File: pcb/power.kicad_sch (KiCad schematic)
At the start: 29 parts, among them J2 USB_C_Top, J3 USB_C_Bottom, Q2 AO3401A, U2 TPS63000, U3 TPS63000, U4 TP4056

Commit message: style: schematics cleanup
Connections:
- net VBUS renamed V_{BUS}
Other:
- note added: "3.3V"
- note added: "5.0V"
- note added: "Battery Charger"
- note added: "Power Input"
- note added: "Power Sharing"
- moved on the sheet: BT1, C10, C11, C12, C8, C9, J2, J3, L1, L2, R12, R13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

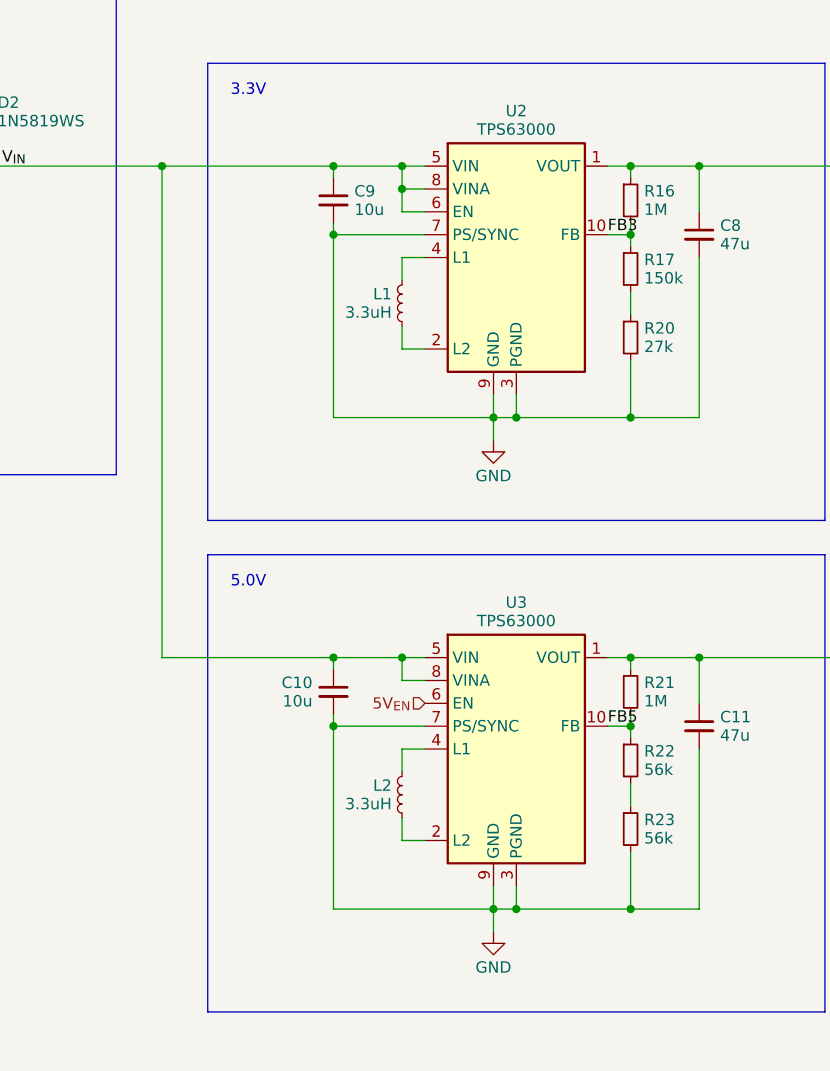
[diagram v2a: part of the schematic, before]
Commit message: style: add 3d models for pcb render
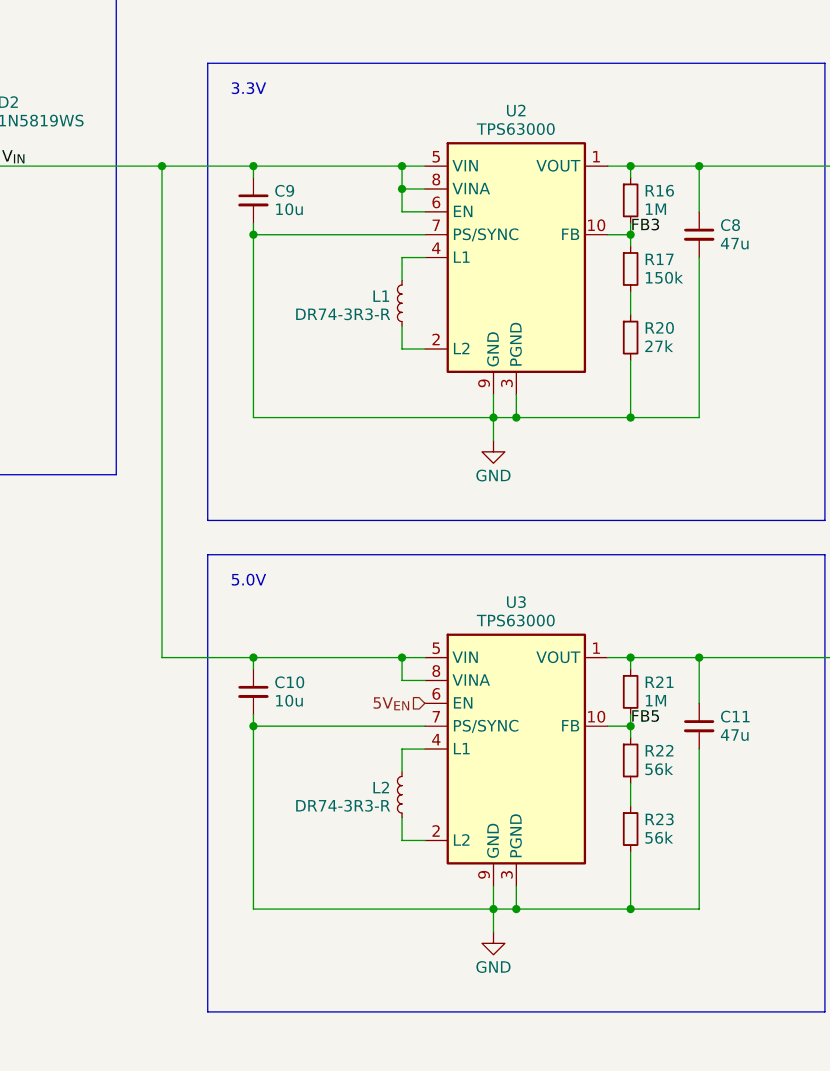
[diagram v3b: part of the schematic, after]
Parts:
- L1, L2: value 3.3uH -> DR74-3R3-R
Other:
- moved on the sheet: C10, C9
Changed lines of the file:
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@@
     (rev "${VERSION}")
   )
-  (junction (at 217.17 49.53) (diameter 0) (color 0 0 0 0)
-  )
   (junction (at 224.79 52.07) (diameter 0) (color 0 0 0 0)
   )
   (junction (at 257.81 104.14) (diameter 0) (color 0 0 0 0)
   )
-  (junction (at 217.17 104.14) (diameter 0) (color 0 0 0 0)
+  (junction (at 208.28 104.14) (diameter 0) (color 0 0 0 0)
+  )
+  (junction (at 208.28 49.53) (diameter 0) (color 0 0 0 0)
   )
   (junction (at 99.06 62.23) (diameter 0) (color 0 0 0 0)
@@
   (junction (at 250.19 57.15) (diameter 0) (color 0 0 0 0)
   )
-  (junction (at 217.17 57.15) (diameter 0) (color 0 0 0 0)
+  (junction (at 208.28 57.15) (diameter 0) (color 0 0 0 0)
   )
   (junction (at 224.79 104.14) (diameter 0) (color 0 0 0 0)
   )
-  (junction (at 217.17 111.76) (diameter 0) (color 0 0 0 0)
+  (junction (at 208.28 111.76) (diameter 0) (color 0 0 0 0)
   )
   (junction (at 234.95 132.08) (diameter 0) (color 0 0 0 0)
@@
     (stroke (width 0) (type default))
   )
-  (wire (pts (xy 217.17 104.14) (xy 198.12 104.14))
+  (wire (pts (xy 208.28 104.14) (xy 198.12 104.14))
     (stroke (width 0) (type default))
   )
@@
     (stroke (width 0) (type default))
   )
-  (wire (pts (xy 247.65 57.15) (xy 250.19 57.15))
-    (stroke (width 0) (type default))
-  )
   (wire (pts (xy 60.96 101.6) (xy 55.88 101.6))
     (stroke (width 0) (type default))
@@
     (stroke (width 0) (type default))
   )
-  (wire (pts (xy 247.65 111.76) (xy 250.19 111.76))
-    (stroke (width 0) (type default))
-  )
   (wire (pts (xy 95.25 46.99) (xy 95.25 49.53))
     (stroke (width 0) (type default))
@@
     (stroke (width 0) (type default))
   )
-  (wire (pts (xy 217.17 57.15) (xy 217.17 77.47))
+  (wire (pts (xy 208.28 57.15) (xy 208.28 77.47))
     (stroke (width 0) (type default))
   )
@@
     (stroke (width 0) (type default))
   )
-  (wire (pts (xy 217.17 49.53) (xy 224.79 49.53))
-    (stroke (width 0) (type default))
-  )
   (wire (pts (xy 177.8 46.99) (xy 177.8 49.53))
     (stroke (width 0) (type default))
@@
     (stroke (width 0) (type default))
   )
-  (wire (pts (xy 217.17 55.88) (xy 217.17 57.15))
+  (wire (pts (xy 208.28 55.88) (xy 208.28 57.15))
     (stroke (width 0) (type default))
   )
@@
     (stroke (width 0) (type default))
   )
-  (wire (pts (xy 217.17 132.08) (xy 234.95 132.08))
+  (wire (pts (xy 208.28 132.08) (xy 234.95 132.08))
     (stroke (width 0) (type default))
   )
@@
     (stroke (width 0) (type default))
   )
-  (wire (pts (xy 217.17 49.53) (xy 217.17 50.8))
+  (wire (pts (xy 208.28 49.53) (xy 208.28 50.8))
     (stroke (width 0) (type default))
   )
@@
     (stroke (width 0) (type default))
   )
-  (wire (pts (xy 217.17 111.76) (xy 217.17 132.08))
+  (wire (pts (xy 250.19 111.76) (xy 247.65 111.76))
+    (stroke (width 0) (type default))
+  )
+  (wire (pts (xy 208.28 111.76) (xy 208.28 132.08))
     (stroke (width 0) (type default))
   )
@@
     (stroke (width 0) (type default))
   )
-  (wire (pts (xy 217.17 104.14) (xy 217.17 105.41))
+  (wire (pts (xy 208.28 104.14) (xy 208.28 105.41))
     (stroke (width 0) (type default))
   )
@@
     (stroke (width 0) (type default))
   )
-  (wire (pts (xy 217.17 111.76) (xy 227.33 111.76))
+  (wire (pts (xy 208.28 111.76) (xy 227.33 111.76))
     (stroke (width 0) (type default))
   )
@@
     (stroke (width 0) (type default))
   )
-  (wire (pts (xy 217.17 110.49) (xy 217.17 111.76))
+  (wire (pts (xy 208.28 110.49) (xy 208.28 111.76))
     (stroke (width 0) (type default))
   )
@@
     (stroke (width 0) (type default))
   )
-  (wire (pts (xy 198.12 49.53) (xy 217.17 49.53))
+  (wire (pts (xy 198.12 49.53) (xy 208.28 49.53))
     (stroke (width 0) (type default))
   )
@@
     (stroke (width 0) (type default))
   )
-  (wire (pts (xy 217.17 77.47) (xy 234.95 77.47))
+  (wire (pts (xy 208.28 77.47) (xy 234.95 77.47))
     (stroke (width 0) (type default))
   )
@@
     (stroke (width 0) (type default))
   )
+  (wire (pts (xy 208.28 49.53) (xy 224.79 49.53))
+    (stroke (width 0) (type default))
+  )
   (wire (pts (xy 119.38 69.85) (xy 119.38 72.39))
     (stroke (width 0) (type default))
   )
+  (wire (pts (xy 250.19 57.15) (xy 247.65 57.15))
+    (stroke (width 0) (type default))
+  )
   (wire (pts (xy 227.33 106.68) (xy 224.79 106.68))
     (stroke (width 0) (type default))
@@
     (stroke (width 0) (type default))
   )
-  (wire (pts (xy 217.17 104.14) (xy 224.79 104.14))
+  (wire (pts (xy 208.28 104.14) (xy 224.79 104.14))
     (stroke (width 0) (type default))
   )
@@
     (stroke (width 0) (type default))
   )
-  (wire (pts (xy 217.17 57.15) (xy 227.33 57.15))
+  (wire (pts (xy 208.28 57.15) (xy 227.33 57.15))
     (stroke (width 0) (type default))
   )
@@
     (effects (font (size 1.27 1.27)) (justify left bottom))
   )
-  (label "FB5" (at 247.65 111.76 0) (fields_autoplaced)
+  (label "FB5" (at 250.19 111.76 0) (fields_autoplaced)
     (effects (font (size 1.27 1.27)) (justify left bottom))
   )
@@
     (effects (font (size 1.27 1.27)) (justify left bottom))
   )
-  (label "FB3" (at 247.65 57.15 0) (fields_autoplaced)
+  (label "FB3" (at 250.19 57.15 0) (fields_autoplaced)
     (effects (font (size 1.27 1.27)) (justify left bottom))
   )
@@
   )
   (symbol (lib_id "Device:L_Small") (at 224.79 119.38 180) (unit 1)
-    (in_bom yes) (on_board yes) (dnp no) (fields_autoplaced)
-    (property "Reference" "L2" (at 223.6493 118.356 0)
-      (effects (font (size 1.27 1.27)) (justify left))
-    )
-    (property "Value" "3.3uH" (at 223.6493 120.404 0)
+    (in_bom yes) (on_board yes) (dnp no)
+    (property "Reference" "L2" (at 223.52 119.38 0)
+      (effects (font (size 1.27 1.27)) (justify left top))
+    )
+    (property "Value" "DR74-3R3-R" (at 223.52 120.65 0)
       (effects (font (size 1.27 1.27)) (justify left))
     )
@@
     )
   )
-  (symbol (lib_id "Device:C_Small") (at 217.17 53.34 0) (unit 1)
-    (in_bom yes) (on_board yes) (dnp no) (fields_autoplaced)
-    (property "Reference" "C9" (at 219.4941 52.3223 0)
-      (effects (font (size 1.27 1.27)) (justify left))
-    )
-    (property "Value" "10u" (at 219.4941 54.3703 0)
-      (effects (font (size 1.27 1.27)) (justify left))
-    )
-    (property "Footprint" "Capacitor_SMD:C_0603_1608Metric" (at 217.17 53.34 0)
-      (effects (font (size 1.27 1.27)) hide)
-    )
-    (property "Datasheet" "~" (at 217.17 53.34 0)
-      (effects (font (size 1.27 1.27)) hide)
-    )
-    (property "LCSC" "C96446" (at 217.17 53.34 0)
+  (symbol (lib_id "Device:C_Small") (at 208.28 53.34 0) (unit 1)
+    (in_bom yes) (on_board yes) (dnp no) (fields_autoplaced)
+    (property "Reference" "C9" (at 210.6041 52.3223 0)
+      (effects (font (size 1.27 1.27)) (justify left))
+    )
+    (property "Value" "10u" (at 210.6041 54.3703 0)
+      (effects (font (size 1.27 1.27)) (justify left))
+    )
+    (property "Footprint" "Capacitor_SMD:C_0603_1608Metric" (at 208.28 53.34 0)
+      (effects (font (size 1.27 1.27)) hide)
+    )
+    (property "Datasheet" "~" (at 208.28 53.34 0)
+      (effects (font (size 1.27 1.27)) hide)
+    )
+    (property "LCSC" "C96446" (at 208.28 53.34 0)
       (effects (font (size 1.27 1.27)) hide)
     )
@@
   )
   (symbol (lib_id "Device:L_Small") (at 224.79 64.77 180) (unit 1)
-    (in_bom yes) (on_board yes) (dnp no) (fields_autoplaced)
-    (property "Reference" "L1" (at 223.6493 63.746 0)
-      (effects (font (size 1.27 1.27)) (justify left))
-    )
-    (property "Value" "3.3uH" (at 223.6493 65.794 0)
+    (in_bom yes) (on_board yes) (dnp no)
+    (property "Reference" "L1" (at 223.52 64.77 0)
+      (effects (font (size 1.27 1.27)) (justify left top))
+    )
+    (property "Value" "DR74-3R3-R" (at 223.52 66.04 0)
       (effects (font (size 1.27 1.27)) (justify left))
     )
@@
     )
   )
-  (symbol (lib_id "Device:C_Small") (at 217.17 107.95 0) (unit 1)
-    (in_bom yes) (on_board yes) (dnp no) (fields_autoplaced)
-    (property "Reference" "C10" (at 214.8459 106.9323 0)
-      (effects (font (size 1.27 1.27)) (justify right))
-    )
-    (property "Value" "10u" (at 214.8459 108.9803 0)
-      (effects (font (size 1.27 1.27)) (justify right))
-    )
-    (property "Footprint" "Capacitor_SMD:C_0603_1608Metric" (at 217.17 107.95 0)
-      (effects (font (size 1.27 1.27)) hide)
-    )
-    (property "Datasheet" "~" (at 217.17 107.95 0)
-      (effects (font (size 1.27 1.27)) hide)
-    )
-    (property "LCSC" "C96446" (at 217.17 107.95 0)
-      (effects (font (size 1.27 1.27)) hide)
-    )
+  (symbol (lib_id "Device:C_Small") (at 208.28 107.95 0) (unit 1)
+    (in_bom yes) (on_board yes) (dnp no) (fields_autoplaced)
+    (property "Reference" "C10" (at 210.6041 106.9323 0)
+      (effects (font (size 1.27 1.27)) (justify left))
+    )
+    (property "Value" "10u" (at 210.6041 108.9803 0)
+      (effects (font (size 1.27 1.27)) (justify left))
+    )
+    (property "Footprint" "Capacitor_SMD:C_0603_1608Metric" (at 208.28 107.95 0)
+      (effects (font (size 1.27 1.27)) hide)
+    )
+    (property "Datasheet" "~" (at 208.28 107.95 0)
+      (effects (font (size 1.27 1.27)) hide)
+    )
+    (property "LCSC" "C96446" (at 208.28 107.95 0)
+      (effects (font (size 1.27 1.27)) hide)
+    )

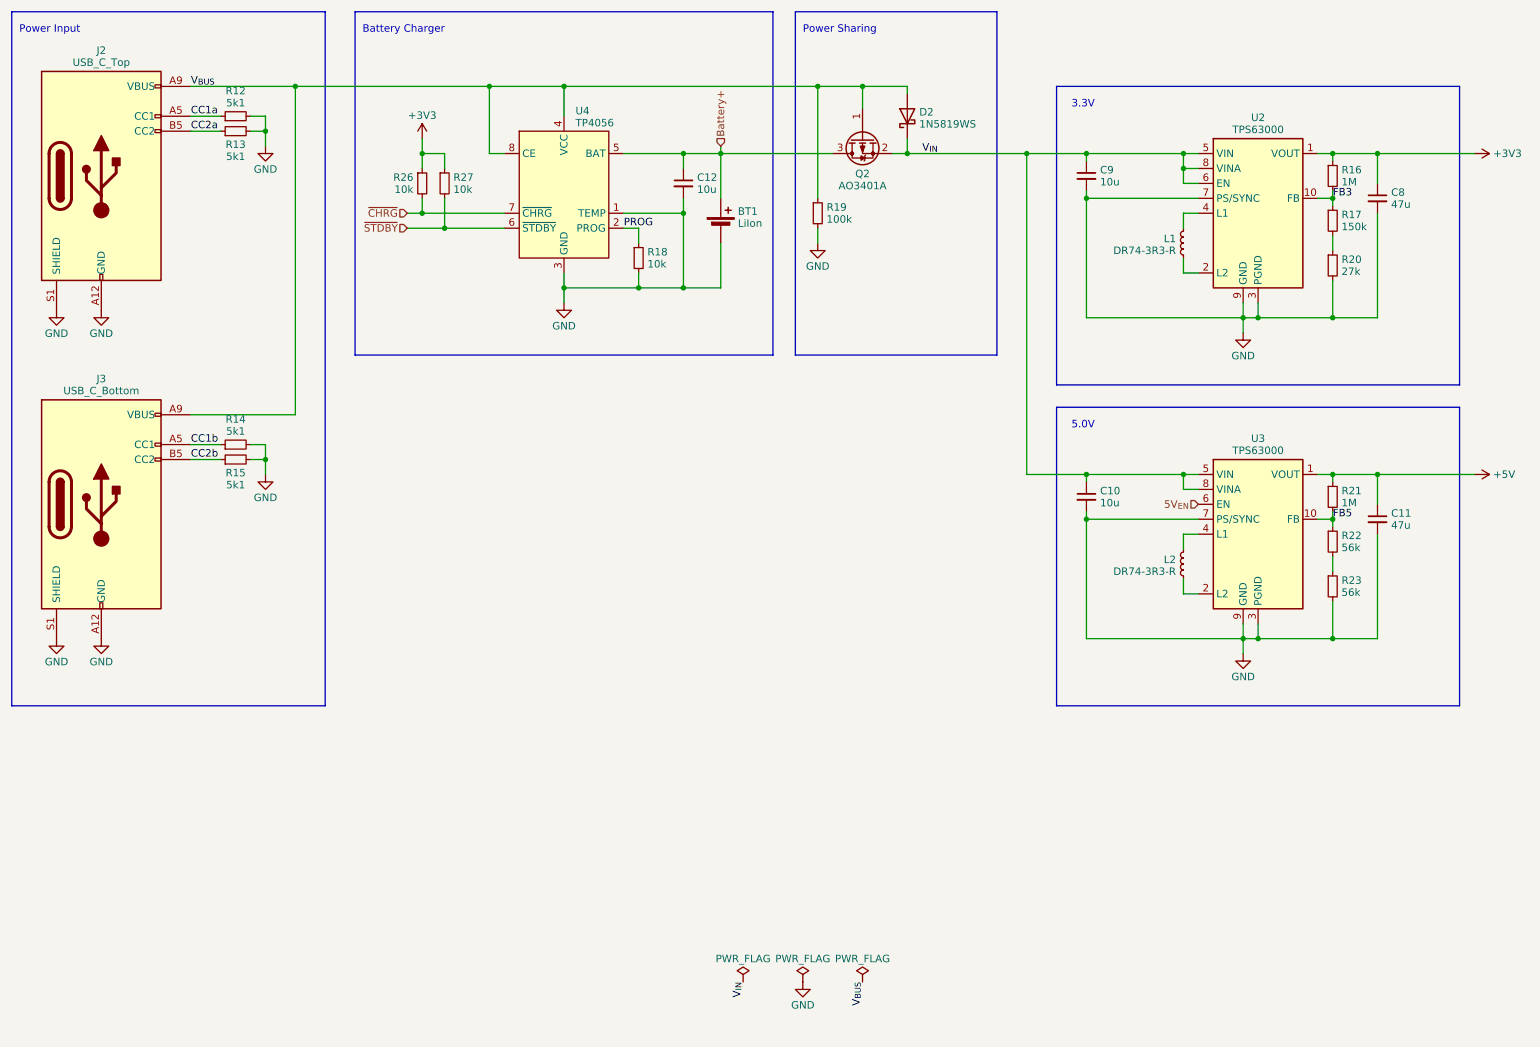
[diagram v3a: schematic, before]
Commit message: feat: add battery protection
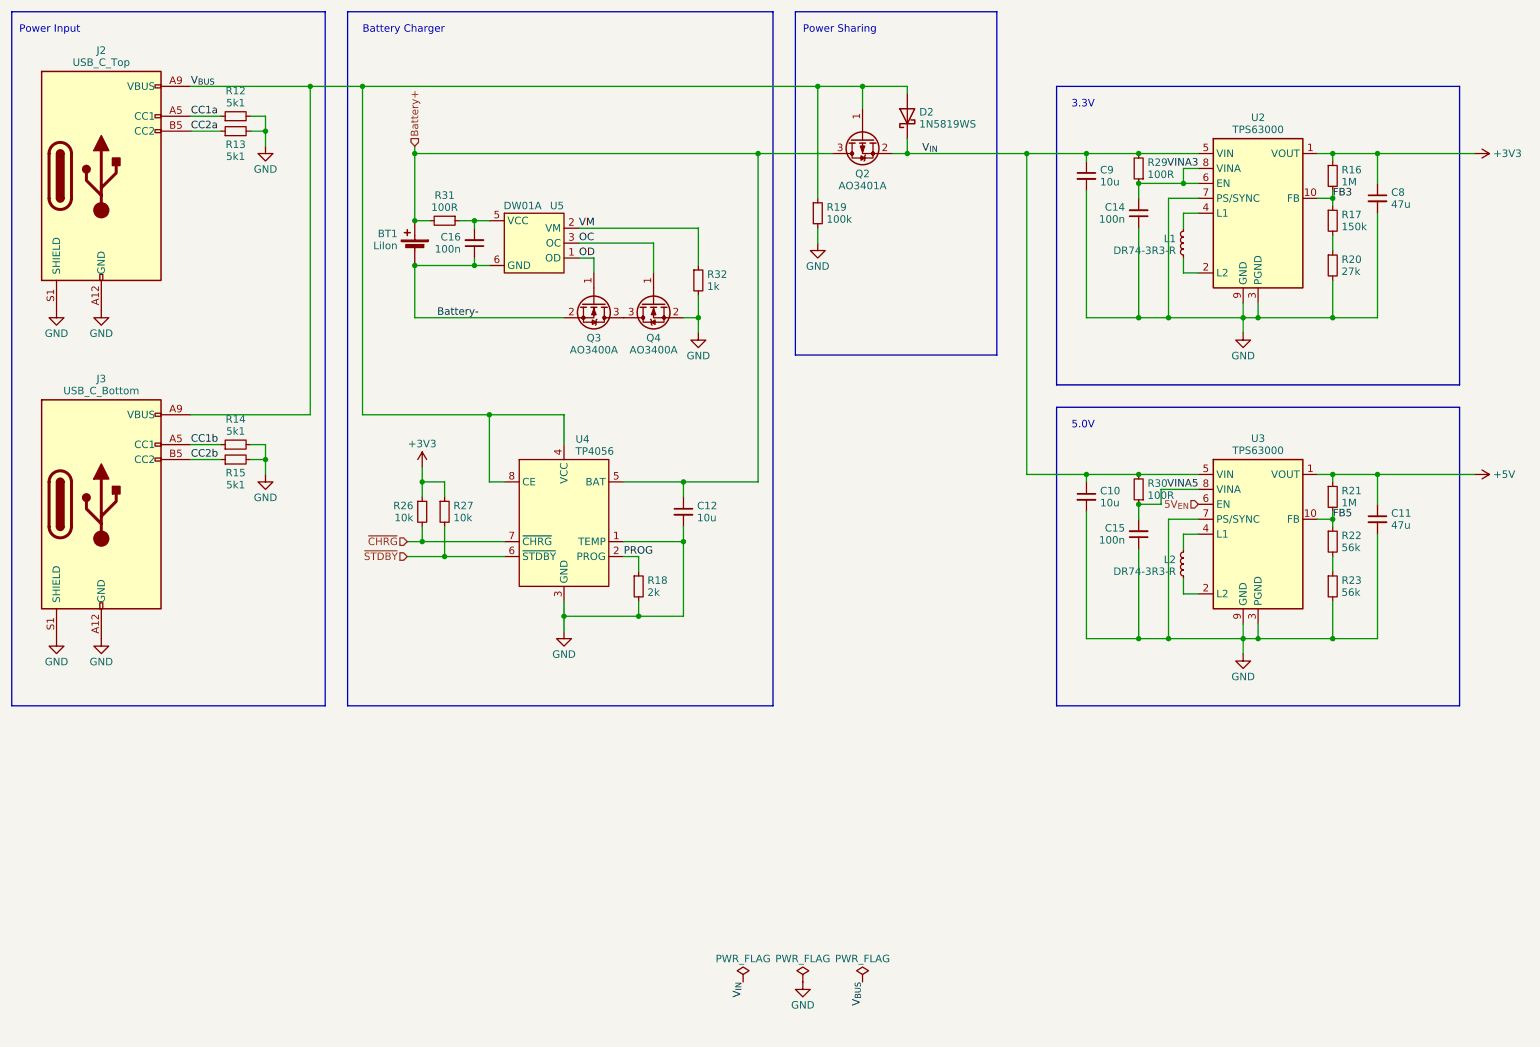
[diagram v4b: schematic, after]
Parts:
- added C14, C15, C16: 100n, Capacitor_SMD:C_0402_1005Metric, symbol Device:C_Small
- added Q3, Q4: AO3400A, Package_TO_SOT_SMD:SOT-23, symbol Transistor_FET:AO3400A
- added R29, R30, R31: 100R, Resistor_SMD:R_0402_1005Metric, symbol Device:R_Small
- added R32: 1k, Resistor_SMD:R_0402_1005Metric, symbol Device:R_Small
- added U5: DW01A, Package_TO_SOT_SMD:SOT-23-6, symbol My_Symbols:DW01A
- R18: value 10k -> 2k
- U2, U3: footprint Package_SON:Texas_DRC0010J -> Package_SON:Texas_DRC0010J_ThermalVias
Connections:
- net Battery+: now also R31.2
- net GND: now also C14.1, C15.1, Q4.2 (S), R32.2; no longer BT1.2 (-)
- net V_{IN}: now also R29.2, R30.2; no longer U2.6 (EN), U2.8 (VINA), U3.8 (VINA)
- new net: C16.2, R31.1, U5.5 (VCC)
- new net: Q3.3 (D), Q4.3 (D)
- new net Battery-: BT1.2 (-), C16.1, Q3.2 (S), U5.6 (GND)
- new net OC: Q4.1 (G), U5.3 (OC)
- new net OD: Q3.1 (G), U5.1 (OD)
- new net VINA3: C14.2, R29.1, U2.6 (EN), U2.8 (VINA)
- new net VINA5: C15.2, R30.1, U3.8 (VINA)
- new net VM: R32.1, U5.2 (VM)
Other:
- moved on the sheet: BT1, C12, R18, R26, R27, U4

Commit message: feat: add reverse polarity protection for battery input
just to make sure a reverse connected battery won't kill the circuit
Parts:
- U2, U3: footprint Package_SON:Texas_DRC0010J_ThermalVias -> Package_SON:Texas_DRC0010J
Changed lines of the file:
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@@
       (effects (font (size 1.27 1.27)))
     )
-    (property "Footprint" "Package_SON:Texas_DRC0010J_ThermalVias" (at 259.08 128.27 0)
+    (property "Footprint" "Package_SON:Texas_DRC0010J" (at 259.08 128.27 0)
       (effects (font (size 1.27 1.27)) hide)
     )
@@
       (effects (font (size 1.27 1.27)))
     )
-    (property "Footprint" "Package_SON:Texas_DRC0010J_ThermalVias" (at 259.08 73.66 0)
-      (effects (font (size 1.27 1.27)) hide)
-    )
+    (property "Footprint" "Package_SON:Texas_DRC0010J" (at 259.08 73.66 0)
+      (effects (font (size 1.27 1.27)) hide)
+    )
